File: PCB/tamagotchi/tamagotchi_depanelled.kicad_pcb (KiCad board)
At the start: 2 copper layers, 23.1 x 68.4 mm, 14 parts, among them J1 Programming port, J2 Conn_01x01_Female, J3 Conn_01x01_Female, J4 Conn_01x01_Male, J5 Conn_01x01_Male, SW1 Main Button, SW2 SW_Push, U1 ATtiny85V-10P, U2 OLED

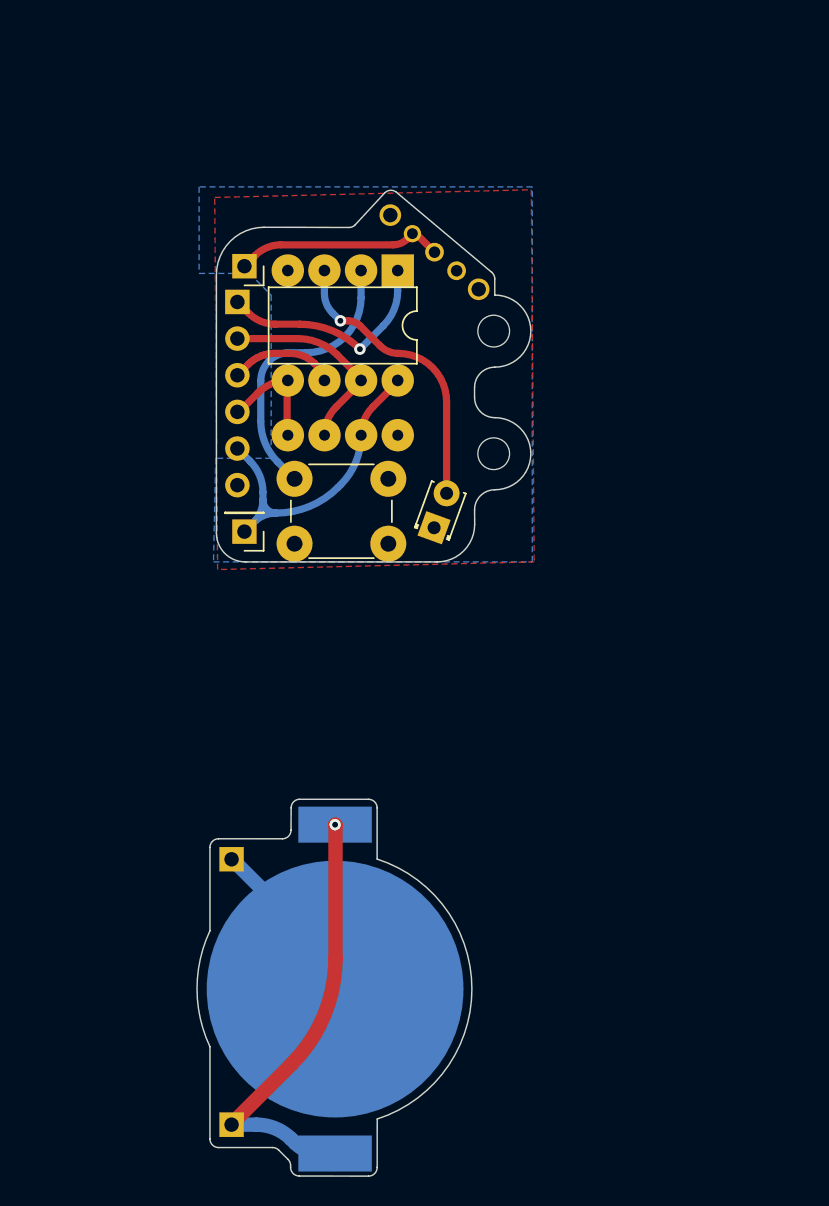
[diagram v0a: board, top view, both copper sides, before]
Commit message: a lot!
okay so gave up on wireframe stuff and instead implemented ageing/hunger. Also added alternate sprites, and started refining the interactivity model
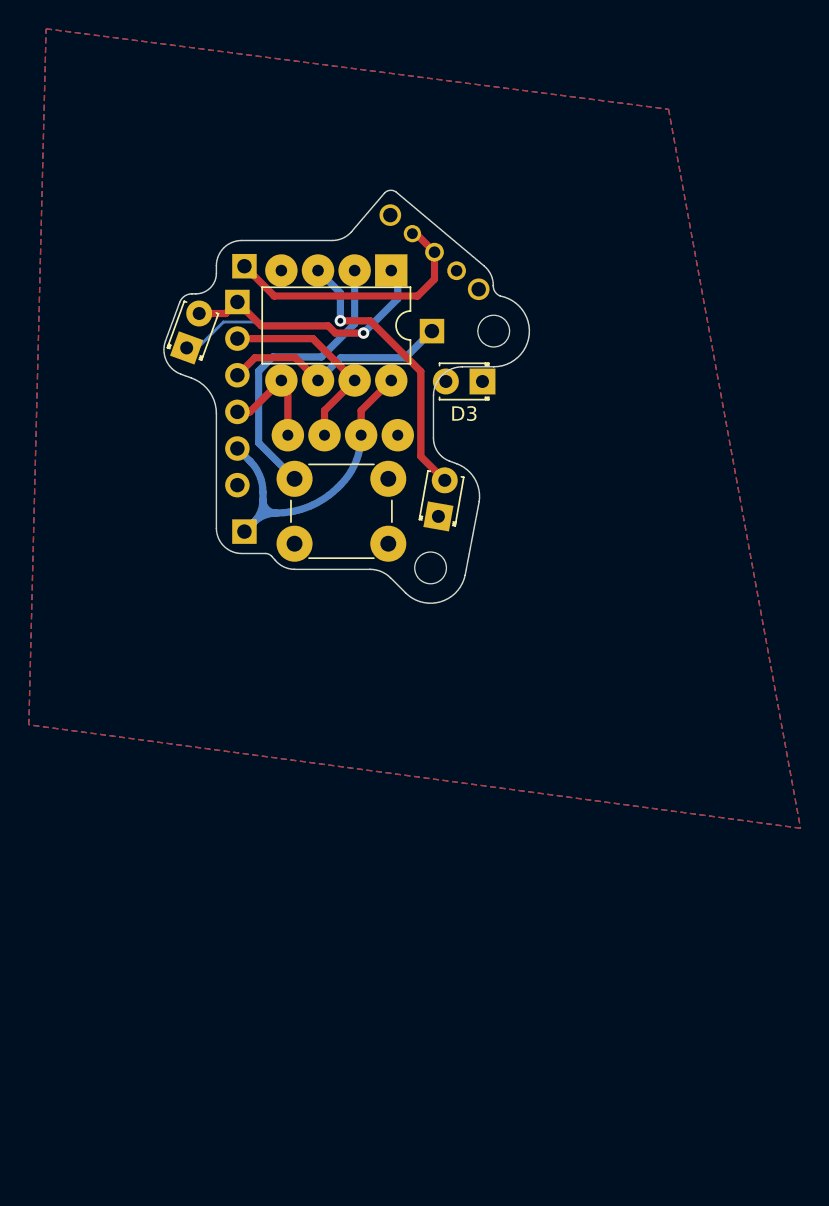
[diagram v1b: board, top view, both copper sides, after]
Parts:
- removed BT2: lr44, Stepchild:Battery Clip
- removed J4, J5: Conn_01x01_Male, Connector_PinHeader_2.54mm:PinHeader_1x01_P2.54mm_Vertical
- added D2: LED, LED_THT:LED_D1.8mm_W3.3mm_H2.4mm, F.Cu at (25.0, 57.3)
- added D3: LED, LED_THT:LED_D1.8mm_W3.3mm_H2.4mm, F.Cu at (45.5, 59.7)
- added J6: Conn_01x01_Female, Connector_PinHeader_2.54mm:PinHeader_1x01_P2.54mm_Vertical, B.Cu at (42.0, 56.2)
- J2, J3: moved to B.Cu
- moved G*** 10.5 mm to (35.7, 68.7)
- moved H2 9.05 mm to (41.9, 72.6)
- moved D1 0.84 mm to (42.4, 69.0), turned to 80 degrees
- moved U1 0.45 mm to (39.2, 52.0)
- turned J2 to 0 degrees
- turned J3 to 0 degrees
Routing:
- net Net-(BT2-+): track 31.0 -> 0.00 mm, vias 1 -> 0
- net Net-(BT2--): track 11.9 -> 0.00 mm
- net ISP MISO: track 7.50 -> 16.1 mm
- net GND: track 0.00 -> 5.14 mm
- net Net-(J3-Pin_1): track 14.4 -> 18.2 mm
- net ISP RESET: track 15.9 -> 17.9 mm
- net LED: track 20.1 -> 19.4 mm
- net ISP MOSI: track 8.02 -> 7.30 mm
- net BUTTON: track 19.6 -> 20.2 mm
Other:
- board size 23.1 x 68.4 mm -> 25.3 x 28.6 mm
- board text removed: "PCB3D_BR_BATTERY"
- board text removed: "PCB3D_BR_MAIN"
- board text removed: "PCB3D_STACK_MAIN_ONTO_BATTERY_2"
- board text removed: "PCB3D_TL_BATTERY"
- board text removed: "PCB3D_TL_MAIN"

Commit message: idk
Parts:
- removed D3: LED, LED_THT:LED_D1.8mm_W3.3mm_H2.4mm
- moved D1 4.94 mm to (41.6, 73.9), turned to 55 degrees
- moved H2 4.89 mm to (45.2, 69.0), turned to -25 degrees
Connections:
- D2 pad 2: ISP RESET -> ISP MISO
- J6 pad 1: ISP MISO -> unconnected-(J6-Pin_1-Pad1)
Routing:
- net LED: track 19.4 -> 24.3 mm
- net ISP MISO: track 16.1 -> 12.1 mm
- net ISP RESET: track 17.9 -> 15.0 mm
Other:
- board size 25.3 x 28.6 mm -> 25.3 x 29 mm
